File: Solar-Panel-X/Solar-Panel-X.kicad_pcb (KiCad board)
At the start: 6 copper layers, 48.4 x 48.4 mm, 63 parts, among them J1 FFC2B28-10-G, U1 TSL2561, U2 BQ25570RGRR

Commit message: Exported Gerbers
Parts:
- added H1: MountingHole, MountingHole:MountingHole_2.2mm_M2_DIN965, F.Cu at (87.5, 49.4)
- added H2: MountingHole, MountingHole:MountingHole_2.2mm_M2_DIN965, F.Cu at (87.5, 83.8)
- added H3: MountingHole, MountingHole:MountingHole_2.2mm_M2_DIN965, F.Cu at (127.3, 83.8)
- added H4: MountingHole, MountingHole:MountingHole_2.2mm_M2_DIN965, F.Cu at (127.3, 49.4)
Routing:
- net /coil: track 12829.8 -> 12851.8 mm
- net SDA1: track 18.4 -> 19.1 mm
- net SCL1: track 16.7 -> 17.3 mm
- net GND: vias 4 -> 3
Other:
- outline, holes or cut-outs redrawn

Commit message: X board updates
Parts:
- removed C14: 100uF, Capacitor_SMD:C_0603_1608Metric
- removed the R17 at (110.8, 53.8)
- removed the R18 at (111.9, 53.8)
- added Q1: BSS138DWQ-7, Package_TO_SOT_SMD:SOT-363_SC-70-6, B.Cu at (102.9, 77.2)
- added Q2: MBT2222ADW1T1, Package_TO_SOT_SMD:SOT-363_SC-70-6, B.Cu at (102.9, 80.0)
- added Q3: BSS138DWQ-7, Package_TO_SOT_SMD:SOT-363_SC-70-6, B.Cu at (96.4, 77.1)
- added Q4: MBT2222ADW1T1, Package_TO_SOT_SMD:SOT-363_SC-70-6, B.Cu at (96.4, 80.0)
- added R20: 680, Resistor_SMD:R_0402_1005Metric, B.Cu at (105.0, 79.0)
- added R21: 100K, Resistor_SMD:R_0402_1005Metric, B.Cu at (100.1, 76.2)
- added R22: 0, Resistor_SMD:R_0402_1005Metric, B.Cu at (102.9, 82.1)
- added R23: 0, Resistor_SMD:R_0402_1005Metric, B.Cu at (96.4, 82.0)
- added R24: 10K, Resistor_SMD:R_0402_1005Metric, B.Cu at (100.1, 77.3)
- added R25: 10K, Resistor_SMD:R_0402_1005Metric, B.Cu at (100.1, 80.3)
- added R26: 200K, Resistor_SMD:R_0402_1005Metric, B.Cu at (100.1, 79.3)
- added R27: 680, Resistor_SMD:R_0402_1005Metric, B.Cu at (98.6, 79.0)
- added R28: 100K, Resistor_SMD:R_0402_1005Metric, B.Cu at (93.4, 76.2)
- added R29: 10K, Resistor_SMD:R_0402_1005Metric, B.Cu at (93.4, 77.2)
- added R3: 0, Resistor_SMD:R_0402_1005Metric, B.Cu at (102.0, 72.0)
- added R30: 10K, Resistor_SMD:R_0402_1005Metric, B.Cu at (93.4, 80.3)
- added R31: 200K, Resistor_SMD:R_0402_1005Metric, B.Cu at (93.4, 79.3)
- added R4: 0, Resistor_SMD:R_0402_1005Metric, B.Cu at (102.0, 68.2)
- C1: renamed from C5; value 0.1uF -> 1uF; moved to F.Cu
- C11: value 100uF -> 0.1uF; footprint Capacitor_SMD:C_0603_1608Metric -> Capacitor_SMD:C_0402_1005Metric
- C12: value 100uF -> 10nF; footprint Capacitor_SMD:C_0603_1608Metric -> Capacitor_SMD:C_0402_1005Metric
- C13: value 0.1uF -> 10nF
- C5: renamed from C6; footprint Capacitor_SMD:C_0402_1005Metric -> Capacitor_SMD:C_0805_2012Metric
- C6: renamed from C1; value 1.0uF -> 1uF
- D1: value SDM20U40-7 -> SZMM5Z5V1T1G
- D4, D5: value SBDiode -> MSS1P4-M3_89A; footprint solarpanels:SB Diode -> solarpanels:MICROSMP
- H1, H2, H3, H4: moved to B.Cu
- J1: value FFC2B28-10-G -> TODO; footprint solarpanels:GCT_FFC2B28-10-G -> Connector_PinHeader_1.27mm:PinHeader_2x05_P1.27mm_Vertical_SMD
- R1: renamed from R12; moved to F.Cu
- R2: renamed from R13; moved to F.Cu
- moved REF** 45.5 mm to (128.9, 88.7) (x2)
- moved REF** 42.3 mm to (106.7, 47.7)
- moved U2 41.2 mm to (106.7, 87.2), turned to 180 degrees
- moved H2 40.2 mm to (99.1, 45.3), turned to 180 degrees
- moved H4 38.8 mm to (120.9, 87.7), turned to 180 degrees
- moved R1 37.6 mm to (109.8, 88.2), turned to -90 degrees
- moved R2 36.4 mm to (109.8, 86.2), turned to -90 degrees
- moved C1 35.8 mm to (110.8, 87.2), turned to -90 degrees
- moved H1 33.7 mm to (120.9, 45.3), turned to 180 degrees
- moved H3 33.4 mm to (94.1, 87.7), turned to 180 degrees
- moved SC5 31.1 mm to (108.2, 78.7)
- moved C13 28.2 mm to (93.4, 78.2), turned to 180 degrees
- moved D3 27.5 mm to (120.3, 66.7), turned to 0 degrees
- moved C10 25.7 mm to (121.2, 82.0), turned to -90 degrees
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- renumbered C8 to C7, C7 to C8, R2 to R12, R3 to R13, R4 to R17, R19 to R18, R1 to R19, U2 to U1, U1 to U2
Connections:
- C11 pad 1: Net-(C11-Pad1) -> +3V3
- C12 pad 1: Net-(C10-Pad1) -> Net-(C12-Pad1)
- C13 pad 1: +3V3 -> Net-(C13-Pad1)
- C7 pad 1: Net-(C11-Pad1) -> Net-(C7-Pad1)
- C9 pad 1: Net-(C11-Pad1) -> Net-(C7-Pad1)
- D3 pad 1: VSOLAR -> Net-(D3-Pad1)
- D3 pad 2: /VSOLAR_FULL -> GND
- D4 pad 2: Net-(D4-Pad2) -> Net-(D3-Pad1)
- D5 pad 1: Net-(D4-Pad2) -> VSOLAR
- D5 pad 2: GND -> /VSOLAR_FULL
- J1 pad 10: COIL_P -> GND
- J1 pad 3: SDA1 -> BURN1
- J1 pad 4: SCL1 -> BURN2
- J1 pad 5: BURN1 -> COIL_P
- J1 pad 6: +3V3 -> COIL_N
- J1 pad 7: GND -> SDA2
- J1 pad 8: GND -> SCL2
- J1 pad 9: COIL_N -> +3V3
- R16 pad 1: Net-(C11-Pad1) -> Net-(C7-Pad1)
- SC1 pad 2: Net-(D4-Pad2) -> Net-(D3-Pad1)
- SC2 pad 2: Net-(D4-Pad2) -> Net-(D3-Pad1)
- SC3 pad 2: Net-(D4-Pad2) -> Net-(D3-Pad1)
- SC4 pad 2: Net-(D4-Pad2) -> Net-(D3-Pad1)
- SC5 pad 1: Net-(D4-Pad2) -> Net-(D3-Pad1)
- SC6 pad 1: Net-(D4-Pad2) -> Net-(D3-Pad1)
- SC7 pad 1: Net-(D4-Pad2) -> Net-(D3-Pad1)
- SC8 pad 1: Net-(D4-Pad2) -> Net-(D3-Pad1)
- TP1 pad 1: +3V3 -> VSOLAR
- TP3 pad 1: VBAT -> +3V3
- TP4 pad 1: VSOLAR -> VBAT
- U1 pad 19: Net-(C11-Pad1) -> Net-(C7-Pad1)
- U2 pad 4: SCL1 -> SCL_LS
- U2 pad 6: SDA1 -> SDA_LS
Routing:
- net /coil: track 12851.8 -> 13245.7 mm, vias 6 -> 5
- net SCL2: track 0.00 -> 25.7 mm, vias 0 -> 2
- net SDA_LS: track 0.00 -> 24.0 mm, vias 0 -> 1
- net GND: track 9.09 -> 28.1 mm, vias 3 -> 11
- net SDA1: track 19.1 -> 0.00 mm, vias 2 -> 0
- net SCL1: track 17.3 -> 0.00 mm, vias 2 -> 0
- net COIL_P: track 23.8 -> 7.60 mm
- net SCL_LS: track 0.00 -> 13.8 mm, vias 0 -> 1
- net Net-(D3-Pad1): track 0.00 -> 13.4 mm, vias 0 -> 6
- net SDA2: track 0.00 -> 12.3 mm, vias 0 -> 2
- net VSOLAR: track 12.2 -> 22.8 mm
- net VBAT: track 20.2 -> 30.7 mm
- net COIL_N: track 21.2 -> 10.7 mm
- net Net-(Q3-Pad6): track 0.00 -> 9.57 mm, vias 0 -> 2
- net Net-(Q1-Pad6): track 0.00 -> 8.89 mm
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- added copper zone on In2.Cu, net +3V3
- added copper zone on In3.Cu, net GND
- added copper zone on B.Cu, net Net-(C7-Pad1)
- added copper zone on F.Cu, net Net-(D3-Pad1)
- removed copper zone on B.Cu, net Net-(C11-Pad1)
- removed copper zone on F.Cu, net Net-(D4-Pad2)
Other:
- board text added: "Cable Pinout 1.BATT_P 2.VUSB 3.BURN1 4.BURN2 5.COIL_P 6.COIL_N 7.SDA 8.SCL 9.+3V3 10.GND"
- board text removed: "1"
- board text removed: "Cable Pinout 1.BATT_P 2.BATT_N 3.SDA 4.SCL 5.BURN 6.3V3 7.GND 8.GND 9.COIL_N 10.COIL_P"

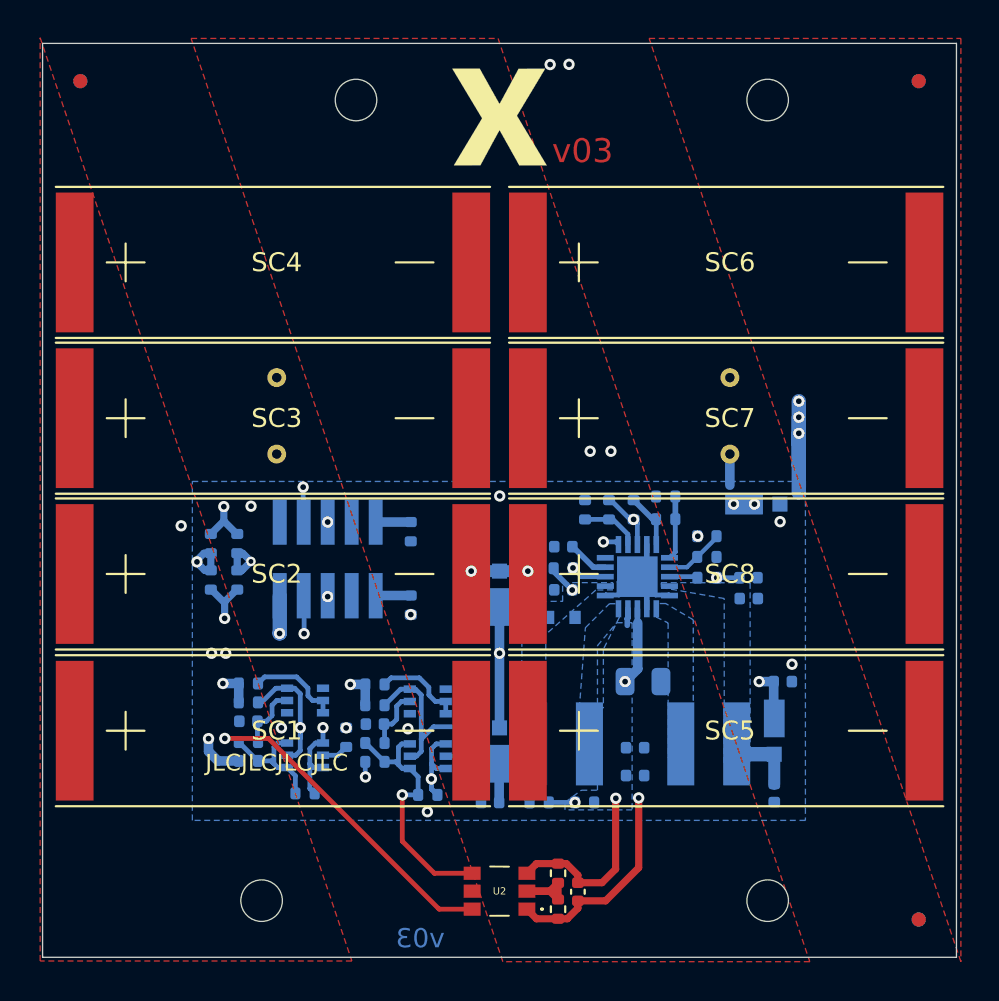
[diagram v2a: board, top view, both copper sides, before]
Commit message: X / Y+ board updates v04
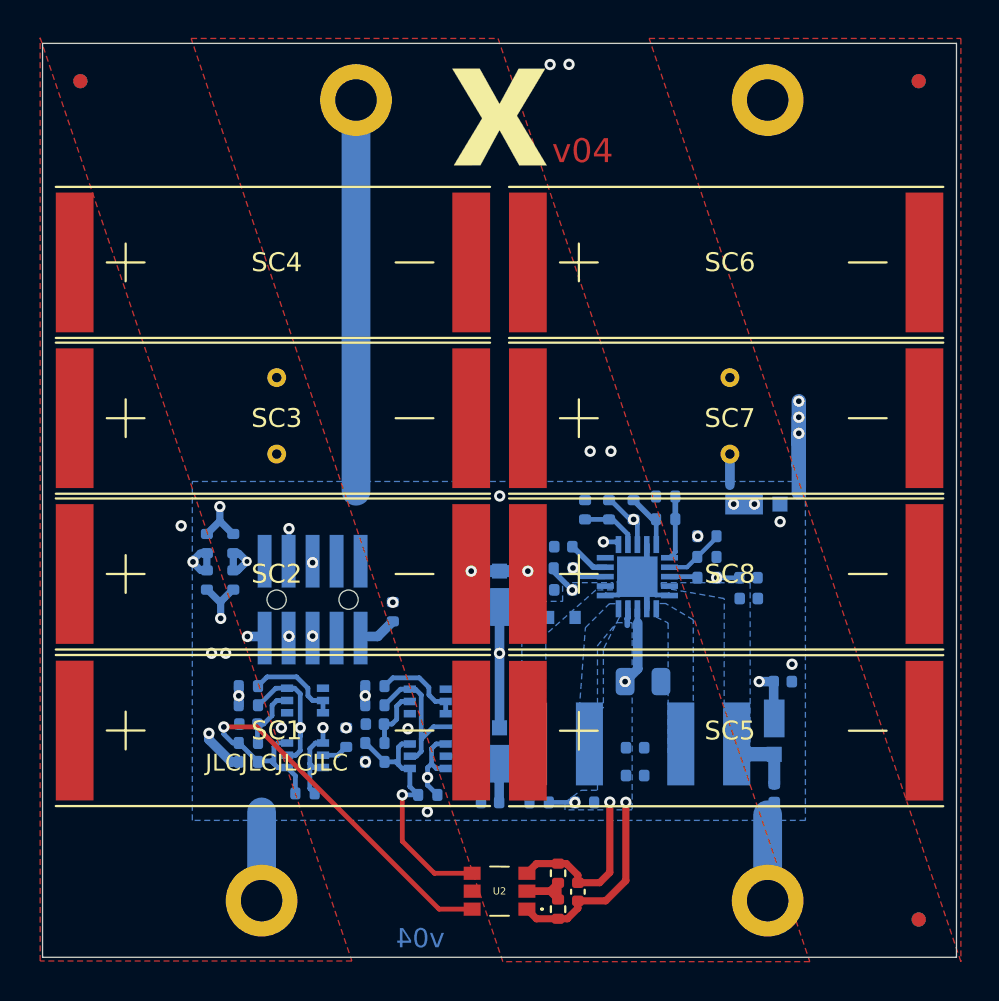
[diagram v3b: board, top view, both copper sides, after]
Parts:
- removed R4: 0, Resistor_SMD:R_0402_1005Metric
- H1, H2, H3, H4: footprint MountingHole:MountingHole_2.2mm_M2_DIN965 -> MountingHole:MountingHole_2.2mm_M2_DIN965_Pad
- J1: value TODO -> FTS-105-01-L-DV-A; footprint Connector_PinHeader_1.27mm:PinHeader_2x05_P1.27mm_Vertical_SMD -> batteryboard:FTS-105-XX-YY-DV-A
- moved J1 2.30 mm to (96.8, 71.8), turned to 180 degrees
- moved R3 1.01 mm to (101.0, 72.4), turned to 90 degrees
- moved R12 0.21 mm to (92.6, 68.8)
- moved R13 0.21 mm to (92.6, 70.7)
- moved R17 0.21 mm to (91.2, 68.8)
- moved R18 0.21 mm to (91.2, 70.7)
- moved C13 0.15 mm to (93.4, 78.3)
- moved R29 0.15 mm to (93.4, 77.3)
- moved R28 0.14 mm to (93.4, 76.3)
- moved R21 0.09 mm to (100.1, 76.3)
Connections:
- J1 pad 2: BATT_N -> VUSB
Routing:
- net GND: track 28.1 -> 55.6 mm, vias 11 -> 10
- net +3V3: track 30.7 -> 25.7 mm
- net /coil: track 13245.7 -> 13249.5 mm
- net SCL2: track 25.7 -> 22.9 mm
- net COIL_P: track 7.60 -> 9.51 mm
- net BATT_N: track 1.86 -> 0.00 mm
- net SDA2: track 12.3 -> 10.5 mm
- net Net-(C10-Pad1): track 4.60 -> 3.73 mm
- net SDA_LS: track 24.0 -> 24.9 mm
- net COIL_N: track 10.7 -> 9.86 mm
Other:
- board text added: "v04"
- board text removed: "v03"

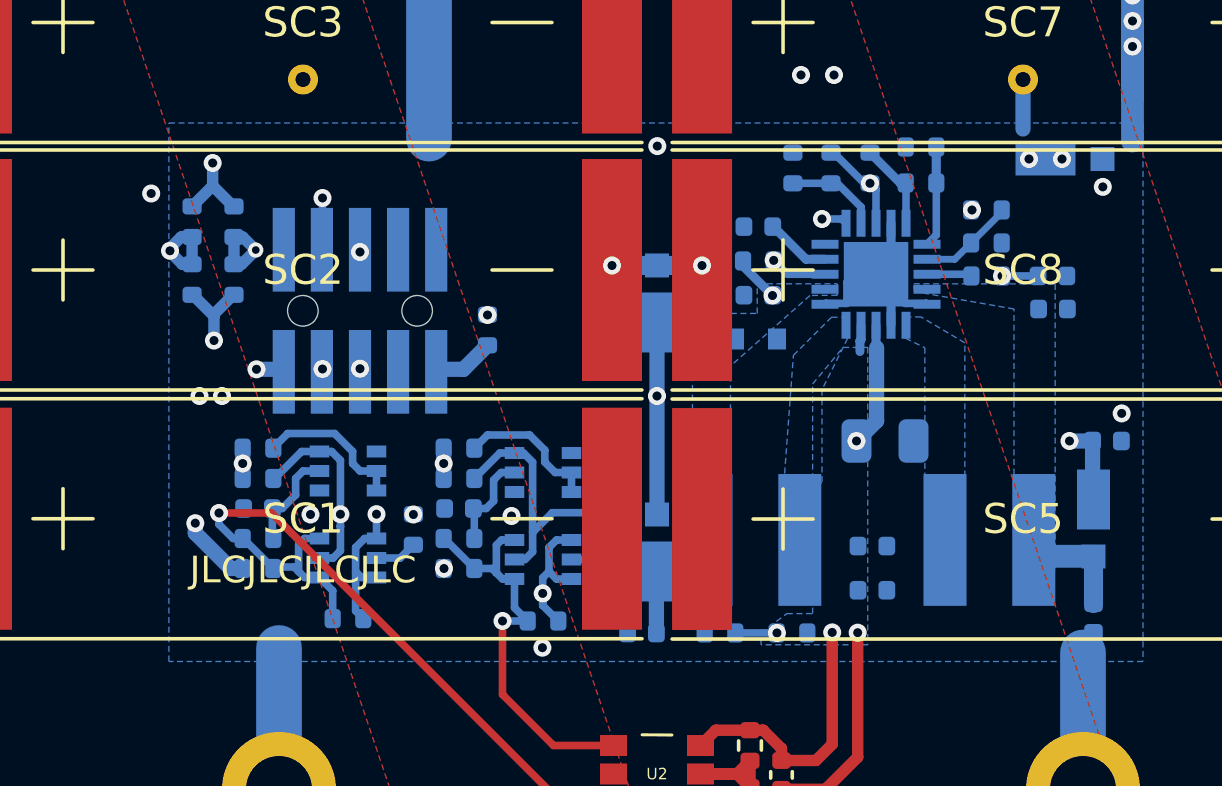
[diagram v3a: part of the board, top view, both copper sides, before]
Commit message: Re-check boards, fixed connector pinouts, moved Y+ connector, re-export models
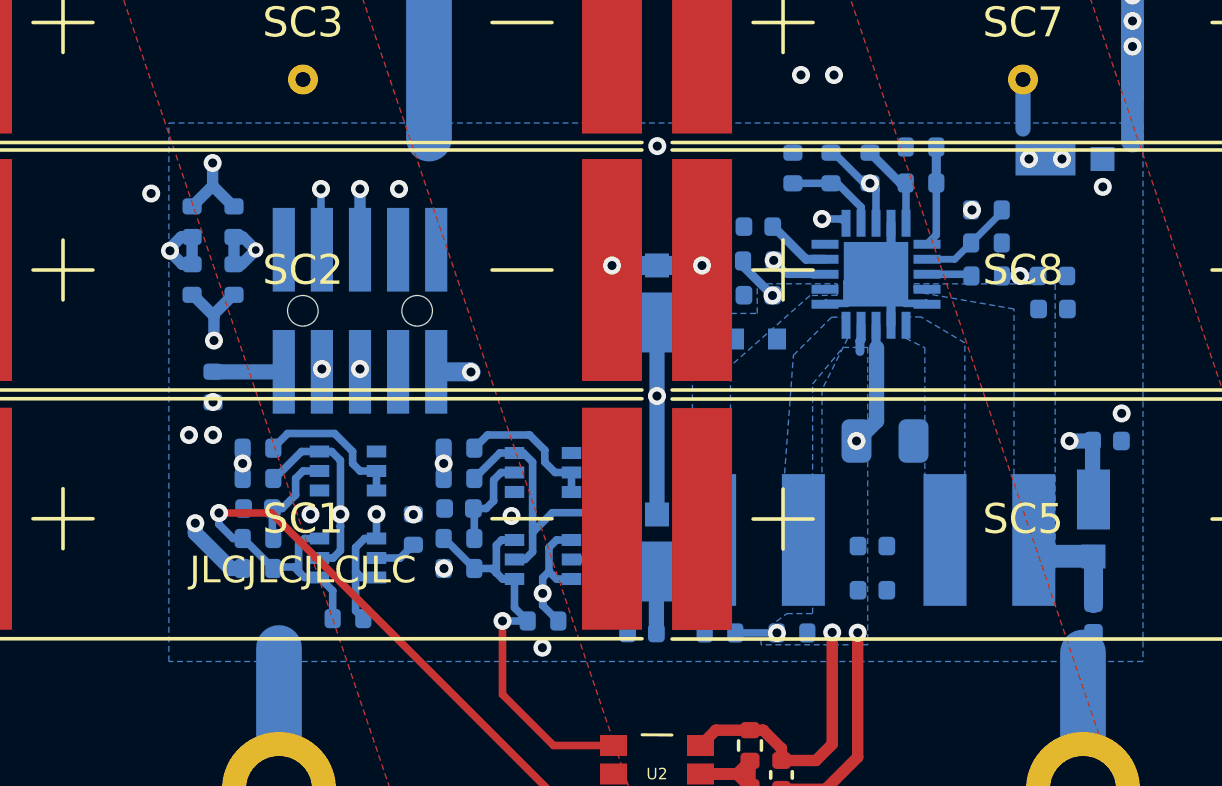
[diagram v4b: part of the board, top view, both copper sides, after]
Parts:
- moved R3 9.35 mm to (91.9, 74.3), turned to -90 degrees
- moved L1 0.12 mm to (110.1, 79.4)
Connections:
- J1 pad 1: BATT_P -> +3V3
- J1 pad 10: GND -> VUSB
- J1 pad 2: VUSB -> GND
- J1 pad 9: +3V3 -> BATT_P
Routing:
- net VBAT: track 30.6 -> 42.9 mm
- net COIL_N: track 9.86 -> 12.8 mm
- net /VSOLAR_FULL: track 21.7 -> 22.5 mm
- net VOUT_EN: track 8.85 -> 9.45 mm
- net SCL2: track 22.9 -> 23.4 mm
- net GND: vias 10 -> 11

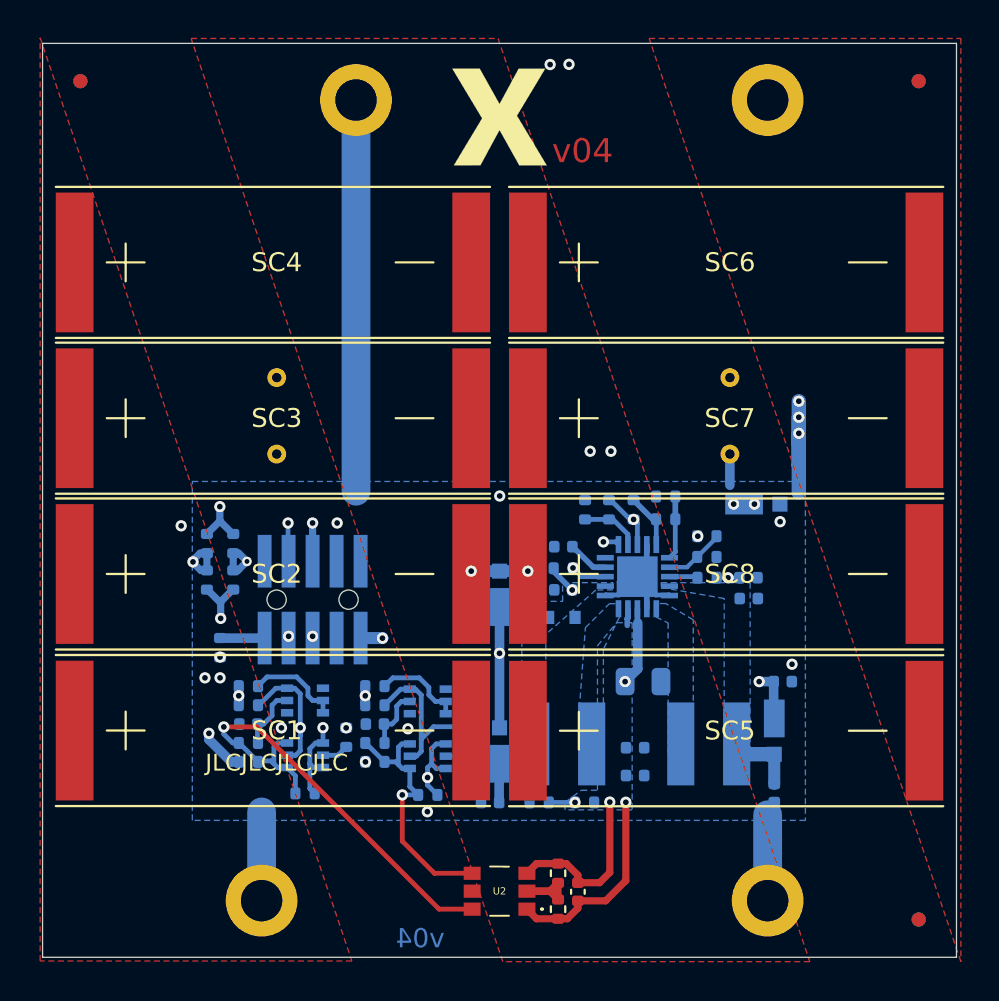
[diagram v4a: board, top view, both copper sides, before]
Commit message: X Board Changes for new Y rails
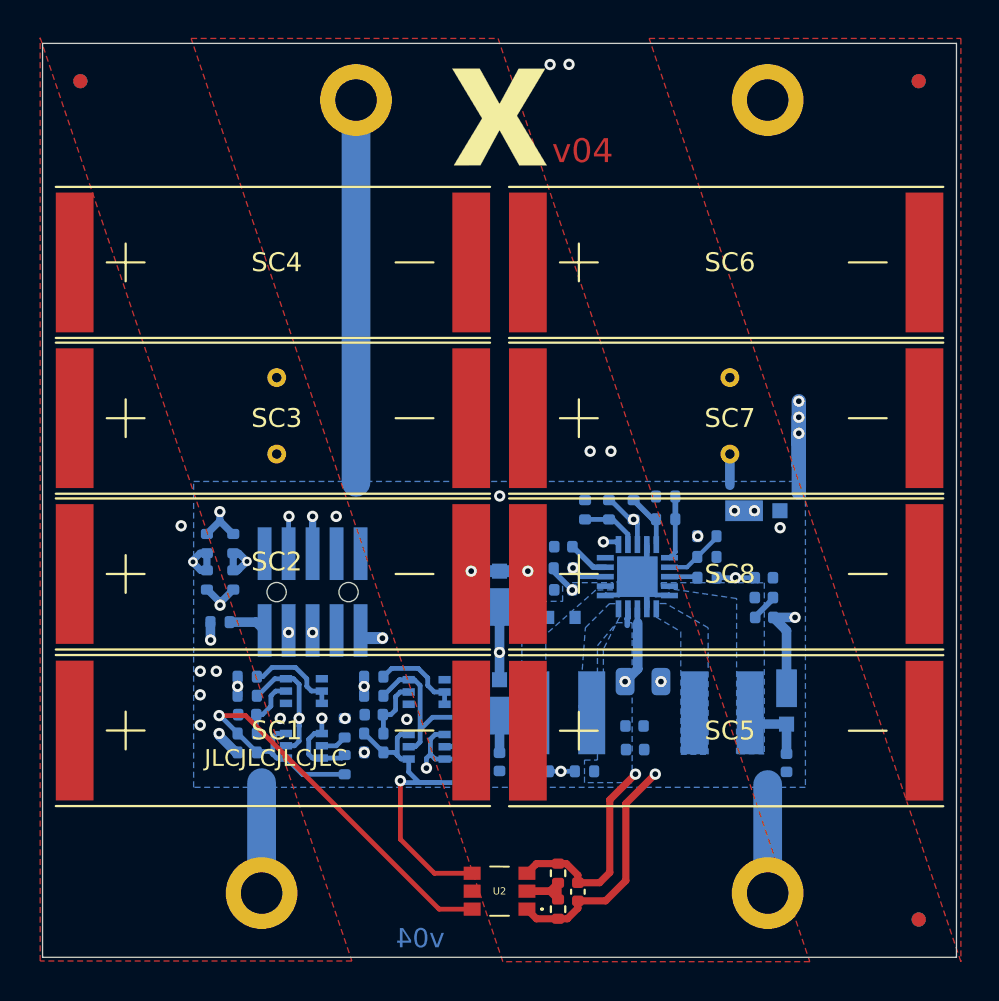
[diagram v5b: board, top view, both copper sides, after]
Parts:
- moved C11 3.54 mm to (120.7, 72.7), turned to 180 degrees
- moved R22 2.67 mm to (105.0, 80.5), turned to 90 degrees
- moved R23 2.59 mm to (98.5, 80.5), turned to 90 degrees
- moved D5 2.55 mm to (106.7, 77.2)
- moved C2 2.21 mm to (106.7, 80.3), turned to -90 degrees
- moved L2 1.80 mm to (118.5, 77.8)
- moved D2 1.73 mm to (121.9, 77.1)
- moved C10 1.73 mm to (121.9, 80.4)
- moved L1 1.65 mm to (110.1, 77.8)
- moved R15 1.65 mm to (108.8, 80.8)
- moved R16 1.65 mm to (111.2, 80.8)
- moved C9 1.37 mm to (113.9, 79.7)
- moved R3 1.35 mm to (91.9, 73.0), turned to 180 degrees
- moved C7 1.15 mm to (113.8, 78.5)
- moved C6 0.82 mm to (120.7, 70.6)
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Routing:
- net /coil: track 13249.5 -> 13219.8 mm
- net GND: track 55.6 -> 60.9 mm, vias 11 -> 12
- net SCL_LS: track 13.8 -> 18.5 mm
- net +3V3: track 25.9 -> 29.6 mm
- net VBAT: track 42.9 -> 46.1 mm
- net /VSOLAR_FULL: track 22.5 -> 20.1 mm
- net SDA_LS: track 24.9 -> 27.3 mm
- net Net-(R14-Pad1): track 16.7 -> 14.7 mm
- net VOUT_EN: track 9.45 -> 10.7 mm
- net SDA2: track 10.5 -> 9.76 mm
